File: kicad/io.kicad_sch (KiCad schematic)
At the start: 7 parts, among them J19 1-wire DS1820, J22 I2C 1, J23 I2C 2, J24 Display

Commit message: kicad: v2 schematic and board update (PCA9685 x2, box-header ports, sensors, analog sockets)
New sheets pwm/powerbar/sensors; Q2/3/5/6 on PCA #1 ch 15-12; sensor GPIOs 5,6,20,21,22,23; 1-Wire +5V_EXT/Data/GND; four identical 0-5 V analog sockets; DC/LED/sensor ports as 2x4 box headers (pin n = Robo-Tank v3 RJ45 pin n). Board: 82 new footprints coarse-placed (56 parked beside the board), ERC 0, DRC copper 0, parity 0. README v2 plan updated.

Co-Authored-By: Claude Opus 5.5 <noreply@anthropic.com>
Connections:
- net +3V3: no longer J19.3 (Pin_3)
- net GND: now also J19.3 (Pin_3); no longer J19.1 (Pin_1)
- new net +5V_EXT: J19.1 (Pin_1)
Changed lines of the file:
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@@
-	)
-	(junction
-		(at 41.91 113.03)
-		(diameter 0)
-		(color 0 0 0 0)
 	)
 	(junction
@@
 	(wire
 		(pts
-			(xy 41.91 124.46) (xy 41.91 123.19)
-		)
-		(stroke
-			(width 0)
-			(type default)
-		)
-	)
-	(wire
-		(pts
-			(xy 41.91 118.11) (xy 38.1 118.11)
-		)
-		(stroke
-			(width 0)
-			(type default)
-		)
-	)
-	(wire
-		(pts
 			(xy 86.36 193.04) (xy 86.36 190.5)
 		)
@@
 		(pts
 			(xy 44.45 193.04) (xy 44.45 190.5)
-		)
-		(stroke
-			(width 0)
-			(type default)
-		)
-	)
-	(wire
-		(pts
-			(xy 41.91 123.19) (xy 38.1 123.19)
-		)
-		(stroke
-			(width 0)
-			(type default)
-		)
-	)
-	(wire
-		(pts
-			(xy 41.91 113.03) (xy 41.91 118.11)
 		)
 		(stroke
@@
 	(symbol
 		(lib_id "power:GND")
-		(at 41.91 124.46 0)
-		(unit 1)
-		(body_style 1)
-		(exclude_from_sim no)
-		(in_bom no)
-		(on_board no)
-		(in_pos_files yes)
-		(dnp no)
-		(property "Reference" "#PWR127"
-			(at 39.37 124.46 0)
-			(hide yes)
-			(show_name no)
-			(do_not_autoplace no)
-			(effects
-				(font
-					(size 1.27 1.27)
-				)
-			)
-		)
-		(property "Value" "GND"
-			(at 44.45 124.46 0)
-			(hide yes)
-			(show_name no)
-			(do_not_autoplace no)
-			(effects
-				(font
-					(size 1.27 1.27)
-				)
-			)
-		)
-		(property "Footprint" ""
-			(at 41.91 124.46 0)
-			(hide yes)
-			(show_name no)
-			(do_not_autoplace no)
-			(effects
-				(font
-					(size 1.27 1.27)
-				)
-			)
-		)
-		(property "Datasheet" ""
-			(at 41.91 124.46 0)
-			(hide yes)
-			(show_name no)
-			(do_not_autoplace no)
-			(effects
-				(font
-					(size 1.27 1.27)
-				)
-			)
-		)
-		(property "Description" "Power symbol creates a global label with name \"GND\" , ground"
-			(at 41.91 124.46 0)
-			(hide yes)
-			(show_name no)
-			(do_not_autoplace no)
-			(effects
-				(font
-					(size 1.27 1.27)
-				)
-			)
-		)
-		(pin "1"
-		)
-		(instances
-			(project "aquaPCB"
-				(path "/80232f81-1179-4777-a7f0-674a974d53cc/69a76064-578d-4a49-aad8-2873571f78bd"
-					(reference "#PWR127")
-					(unit 1)
-				)
-			)
-		)
-	)
-	(symbol
-		(lib_id "power:GND")
 		(at 44.45 261.62 0)
 		(unit 1)
@@
 					(unit 1)
 				)
+			)
+		)
+	)
+	(wire
+		(pts
+			(xy 38.1 123.19) (xy 40.64 123.19)
+		)
+		(stroke
+			(width 0)
+			(type default)
+		)
+	)
+	(global_label "+5V_EXT"
+		(shape bidirectional)
+		(at 40.64 123.19 0)
+		(fields_autoplaced yes)
+		(effects
+			(font
+				(size 1.27 1.27)
+			)
+			(justify left)
+		)
+		(property "Intersheetrefs" "${INTERSHEET_REFS}"
+			(at 40.64 123.19 0)
+			(effects
+				(font
+					(size 1.27 1.27)
+				)
+				(hide yes)
+			)
+		)
+	)
+	(wire
+		(pts
+			(xy 38.1 118.11) (xy 40.64 118.11)
+		)
+		(stroke
+			(width 0)
+			(type default)
+		)
+	)
+	(symbol
+		(lib_id "power:GND")
+		(at 40.64 118.11 90)
+		(unit 1)
+		(body_style 1)
+		(exclude_from_sim no)
+		(in_bom no)
+		(on_board no)
+		(in_pos_files yes)
+		(dnp no)
+		(property "Reference" "#PWR900"
+			(at 38.1 118.11 0)
+			(hide yes)
+			(show_name no)
+			(do_not_autoplace no)
+			(effects
+				(font
+					(size 1.27 1.27)
+				)
+			)
+		)
+		(property "Value" "GND"
+			(at 43.18 118.11 0)
+			(hide yes)
+			(show_name no)
+			(do_not_autoplace no)
+			(effects
+				(font
+					(size 1.27 1.27)
+				)
+			)
+		)
+		(property "Footprint" ""
+			(at 40.64 118.11 0)
+			(hide yes)
+			(show_name no)
+			(do_not_autoplace no)
+			(effects
+				(font
+					(size 1.27 1.27)
+				)
+			)
+		)
+		(property "Datasheet" ""
+			(at 40.64 118.11 0)
+			(hide yes)
+			(show_name no)
+			(do_not_autoplace no)
+			(effects
+				(font
+					(size 1.27 1.27)
+				)
+			)
+		)
+		(property "Description" "Power symbol creates a global label with name \"GND\" , ground"
+			(at 40.64 118.11 0)
+			(hide yes)
+			(show_name no)
+			(do_not_autoplace no)
+			(effects
+				(font
+					(size 1.27 1.27)
+				)
+			)
+		)
+		(pin "1"
+		)
+		(instances
+			(project "aquaPCB"
+				(path "/80232f81-1179-4777-a7f0-674a974d53cc/69a76064-578d-4a49-aad8-2873571f78bd"
+					(reference "#PWR900")
+					(unit 1)
+				)

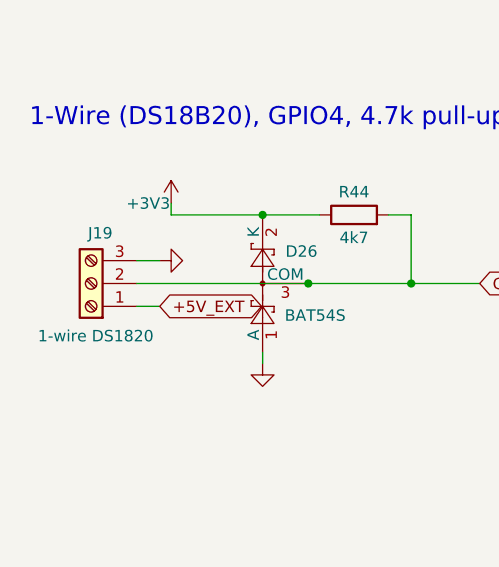
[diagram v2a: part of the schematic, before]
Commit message: kicad: pin headers for 1-Wire, ADC and floats; connectivity-driven re-placement
J19, ADC sockets (J36/J37/J26/J27, 3x4 grid) and floats J30/J31 are pin headers now. All footprints placed on the board (big connectors first, flat parts allowed under the Pi, user-placed U10/RN5/J32/U11 and user routing kept): signal ratsnest 7824 -> 4450 mm, crossings 1776 -> 862. ERC 0, DRC copper 0, parity 0.

Co-Authored-By: Claude Opus 5.5 <noreply@anthropic.com>
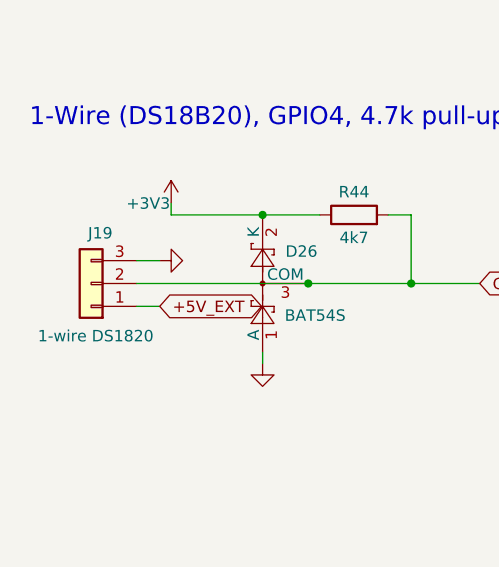
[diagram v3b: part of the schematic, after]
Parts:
- J19: footprint aquaPCB:TerminalBlock_Kangnex_WJ250B-3.5-03P_P3.50mm_Staggered -> Connector_PinHeader_2.54mm:PinHeader_1x03_P2.54mm_Vertical; symbol Connector:Screw_Terminal_01x03 -> Connector_Generic:Conn_01x03; KiLib_Generator terminal_block/Phoenix -> connector/pin_header_socket; LCSC C8420 -> (none)
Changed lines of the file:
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@@
+	(wire
+		(pts
+			(xy 38.1 123.19) (xy 40.64 123.19)
+		)
+		(stroke
+			(width 0)
+			(type default)
+		)
+	)
 	(wire
 		(pts
@@
 	(wire
 		(pts
+			(xy 38.1 118.11) (xy 40.64 118.11)
+		)
+		(stroke
+			(width 0)
+			(type default)
+		)
+	)
+	(wire
+		(pts
 			(xy 52.07 113.03) (xy 58.42 113.03)
 		)
@@
 			(width 0)
 			(type default)
+		)
+	)
+	(global_label "+5V_EXT"
+		(shape bidirectional)
+		(at 40.64 123.19 0)
+		(fields_autoplaced yes)
+		(effects
+			(font
+				(size 1.27 1.27)
+			)
+			(justify left)
+		)
+		(property "Intersheetrefs" "${INTERSHEET_REFS}"
+			(at 40.64 123.19 0)
+			(hide yes)
+			(show_name no)
+			(do_not_autoplace no)
+			(effects
+				(font
+					(size 1.27 1.27)
+				)
+			)
 		)
 	)
@@
 				(font
 					(size 1.27 1.27)
+				)
+			)
+		)
+	)
+	(symbol
+		(lib_id "power:GND")
+		(at 40.64 118.11 90)
+		(unit 1)
+		(body_style 1)
+		(exclude_from_sim no)
+		(in_bom no)
+		(on_board no)
+		(in_pos_files yes)
+		(dnp no)
+		(property "Reference" "#PWR900"
+			(at 38.1 118.11 0)
+			(hide yes)
+			(show_name no)
+			(do_not_autoplace no)
+			(effects
+				(font
+					(size 1.27 1.27)
+				)
+			)
+		)
+		(property "Value" "GND"
+			(at 43.18 118.11 0)
+			(hide yes)
+			(show_name no)
+			(do_not_autoplace no)
+			(effects
+				(font
+					(size 1.27 1.27)
+				)
+			)
+		)
+		(property "Footprint" ""
+			(at 40.64 118.11 0)
+			(hide yes)
+			(show_name no)
+			(do_not_autoplace no)
+			(effects
+				(font
+					(size 1.27 1.27)
+				)
+			)
+		)
+		(property "Datasheet" ""
+			(at 40.64 118.11 0)
+			(hide yes)
+			(show_name no)
+			(do_not_autoplace no)
+			(effects
+				(font
+					(size 1.27 1.27)
+				)
+			)
+		)
+		(property "Description" "Power symbol creates a global label with name \"GND\" , ground"
+			(at 40.64 118.11 0)
+			(hide yes)
+			(show_name no)
+			(do_not_autoplace no)
+			(effects
+				(font
+					(size 1.27 1.27)
+				)
+			)
+		)
+		(pin "1"
+		)
+		(instances
+			(project "aquaPCB"
+				(path "/80232f81-1179-4777-a7f0-674a974d53cc/69a76064-578d-4a49-aad8-2873571f78bd"
+					(reference "#PWR900")
+					(unit 1)
 				)
 			)
@@
 	)
 	(symbol
-		(lib_id "Connector:Screw_Terminal_01x03")
+		(lib_id "Connector_Generic:Conn_01x03")
 		(at 33.02 120.65 180)
 		(unit 1)
@@
 			)
 		)
-		(property "Footprint" "aquaPCB:TerminalBlock_Kangnex_WJ250B-3.5-03P_P3.50mm_Staggered"
+		(property "Footprint" "Connector_PinHeader_2.54mm:PinHeader_1x03_P2.54mm_Vertical"
 			(at 33.02 120.65 0)
 			(hide yes)
@@
 			)
 		)
-		(property "LCSC" "C8420"
+		(property "LCSC" ""
 			(at 33.02 120.65 0)
 			(hide yes)
@@
 			)
 		)
-		(property "KiLib_Generator" "terminal_block/Phoenix"
+		(property "KiLib_Generator" "connector/pin_header_socket"
 			(at 33.02 120.65 0)
 			(hide yes)
@@
 					(unit 1)
 				)
-			)
-		)
-	)
-	(wire
-		(pts
-			(xy 38.1 123.19) (xy 40.64 123.19)
-		)
-		(stroke
-			(width 0)
-			(type default)
-		)
-	)
-	(global_label "+5V_EXT"
-		(shape bidirectional)
-		(at 40.64 123.19 0)
-		(fields_autoplaced yes)
-		(effects
-			(font
-				(size 1.27 1.27)
-			)
-			(justify left)
-		)
-		(property "Intersheetrefs" "${INTERSHEET_REFS}"
-			(at 40.64 123.19 0)
-			(effects
-				(font
-					(size 1.27 1.27)
-				)
-				(hide yes)
-			)
-		)
-	)
-	(wire
-		(pts
-			(xy 38.1 118.11) (xy 40.64 118.11)
-		)
-		(stroke
-			(width 0)
-			(type default)
-		)
-	)
-	(symbol
-		(lib_id "power:GND")
-		(at 40.64 118.11 90)
-		(unit 1)
-		(body_style 1)
-		(exclude_from_sim no)
-		(in_bom no)
-		(on_board no)
-		(in_pos_files yes)
-		(dnp no)
-		(property "Reference" "#PWR900"
-			(at 38.1 118.11 0)
-			(hide yes)
-			(show_name no)
-			(do_not_autoplace no)
-			(effects
-				(font
-					(size 1.27 1.27)
-				)
-			)
-		)
-		(property "Value" "GND"
-			(at 43.18 118.11 0)
-			(hide yes)
-			(show_name no)
-			(do_not_autoplace no)
-			(effects
-				(font
-					(size 1.27 1.27)
-				)
-			)
-		)
-		(property "Footprint" ""
-			(at 40.64 118.11 0)
-			(hide yes)
-			(show_name no)
-			(do_not_autoplace no)
-			(effects
-				(font
-					(size 1.27 1.27)
-				)
-			)
-		)
-		(property "Datasheet" ""
-			(at 40.64 118.11 0)
-			(hide yes)
-			(show_name no)
-			(do_not_autoplace no)
-			(effects
-				(font
-					(size 1.27 1.27)
-				)
-			)
-		)
-		(property "Description" "Power symbol creates a global label with name \"GND\" , ground"
-			(at 40.64 118.11 0)
-			(hide yes)
-			(show_name no)
-			(do_not_autoplace no)
-			(effects
-				(font
-					(size 1.27 1.27)
-				)
-			)
-		)
-		(pin "1"
-		)
-		(instances
-			(project "aquaPCB"
-				(path "/80232f81-1179-4777-a7f0-674a974d53cc/69a76064-578d-4a49-aad8-2873571f78bd"
-					(reference "#PWR900")
-					(unit 1)
-				)
